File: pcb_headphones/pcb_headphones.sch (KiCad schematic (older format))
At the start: 32 parts, among them J1 CONN_01X03, J2 CONN_01X03, J3 CONN_01X03, J4 CONN_01X02, Q1 TIP121, U1 MC34063, U2 TDA2822M

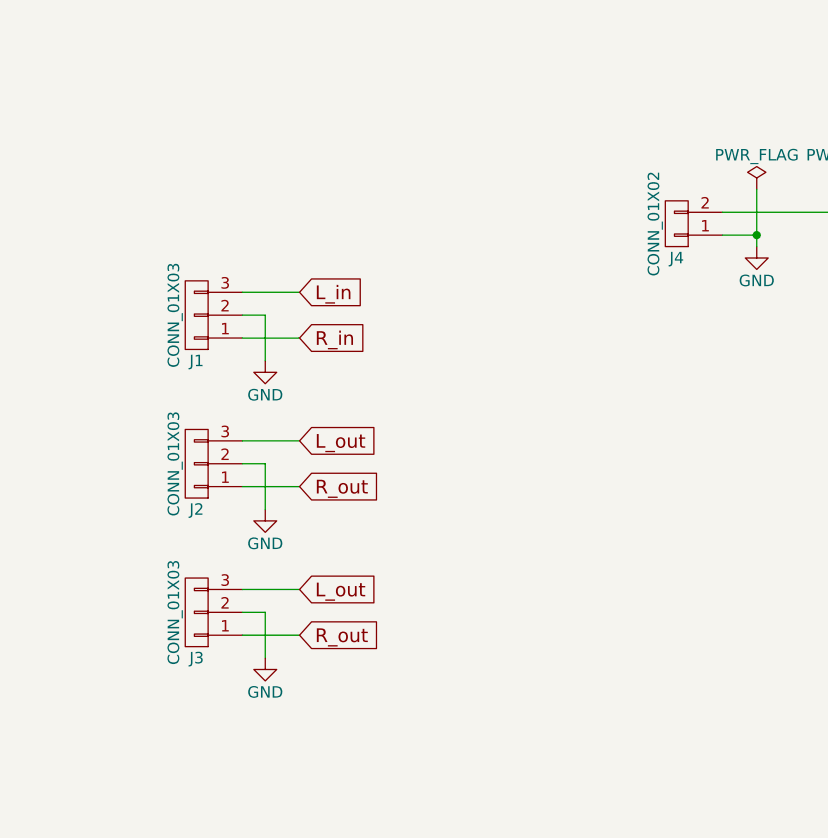
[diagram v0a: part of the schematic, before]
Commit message: Name connectors
Signed-off-by: Jan Losinski <losinski@wh2.tu-dresden.de>
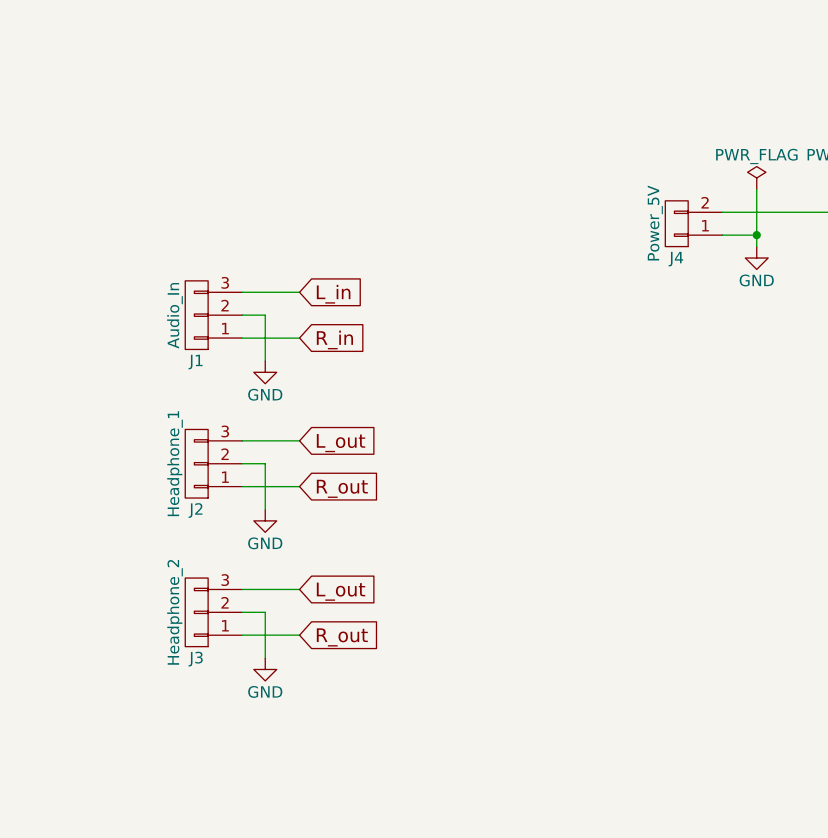
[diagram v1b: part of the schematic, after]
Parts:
- J1: value CONN_01X03 -> Audio_In
- J2: value CONN_01X03 -> Headphone_1
- J3: value CONN_01X03 -> Headphone_2
- J4: value CONN_01X02 -> Power_5V
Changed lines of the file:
@@
 P 6900 3650
 F 0 "J1" H 6900 3850 50  0000 C CNN
-F 1 "CONN_01X03" V 7000 3650 50  0000 C CNN
+F 1 "Audio_In" V 7000 3650 50  0000 C CNN
 F 2 "Pin_Headers:Pin_Header_Straight_1x03" H 6900 3650 50  0001 C CNN
 F 3 "" H 6900 3650 50  0001 C CNN
@@
 P 6900 4300
 F 0 "J2" H 6900 4500 50  0000 C CNN
-F 1 "CONN_01X03" V 7000 4300 50  0000 C CNN
+F 1 "Headphone_1" V 7000 4300 50  0000 C CNN
 F 2 "Pin_Headers:Pin_Header_Straight_1x03" H 6900 4300 50  0001 C CNN
 F 3 "" H 6900 4300 50  0001 C CNN
@@
 P 6900 4950
 F 0 "J3" H 6900 5150 50  0000 C CNN
-F 1 "CONN_01X03" V 7000 4950 50  0000 C CNN
+F 1 "Headphone_2" V 7000 4950 50  0000 C CNN
 F 2 "Pin_Headers:Pin_Header_Straight_1x03" H 6900 4950 50  0001 C CNN
 F 3 "" H 6900 4950 50  0001 C CNN
@@
 P 9000 3250
 F 0 "J4" H 9000 3400 50  0000 C CNN
-F 1 "CONN_01X02" V 9100 3250 50  0000 C CNN
+F 1 "Power_5V" V 9100 3250 50  0000 C CNN
 F 2 "Pin_Headers:Pin_Header_Straight_1x02" H 9000 3250 50  0001 C CNN
 F 3 "" H 9000 3250 50  0001 C CNN

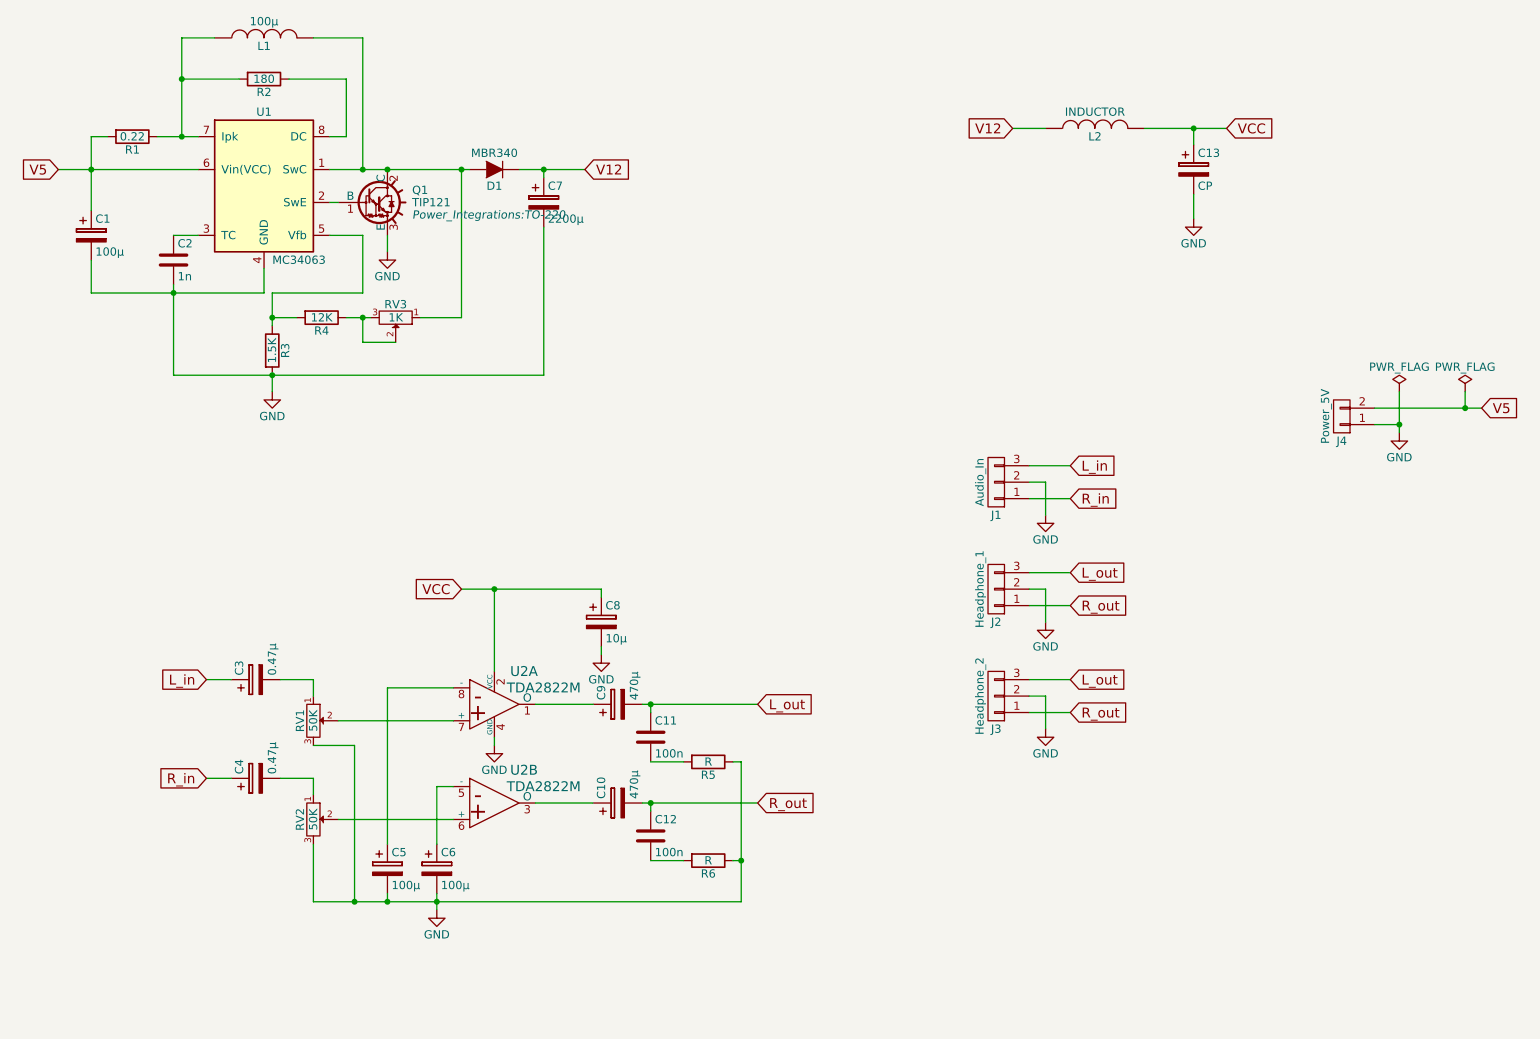
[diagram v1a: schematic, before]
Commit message: Rearange schematic
Signed-off-by: Jan Losinski <losinski@wh2.tu-dresden.de>
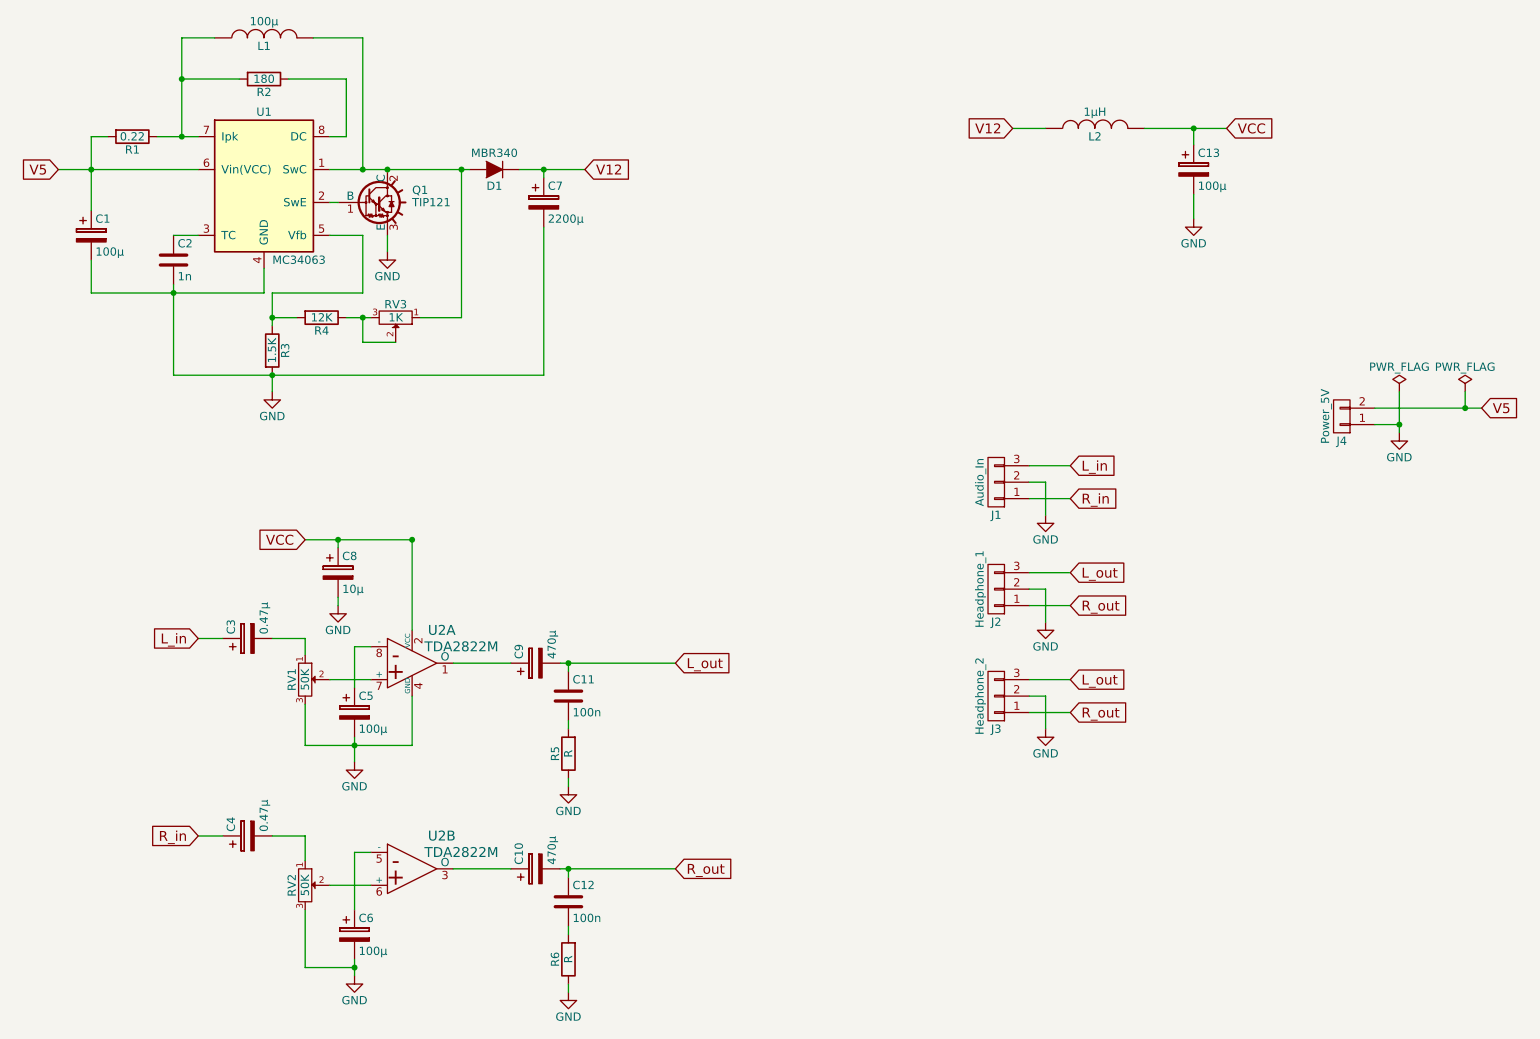
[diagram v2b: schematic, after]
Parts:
- C13: value CP -> 100µ
- L2: value INDUCTOR -> 1µH
- Q1: footprint Power_Integrations:TO-220 -> TO_SOT_Packages_THT:TO-220_Neutral123_Vertical
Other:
- moved on the sheet: C10, C11, C12, C3, C4, C5, C6, C8, C9, R5, R6, RV1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

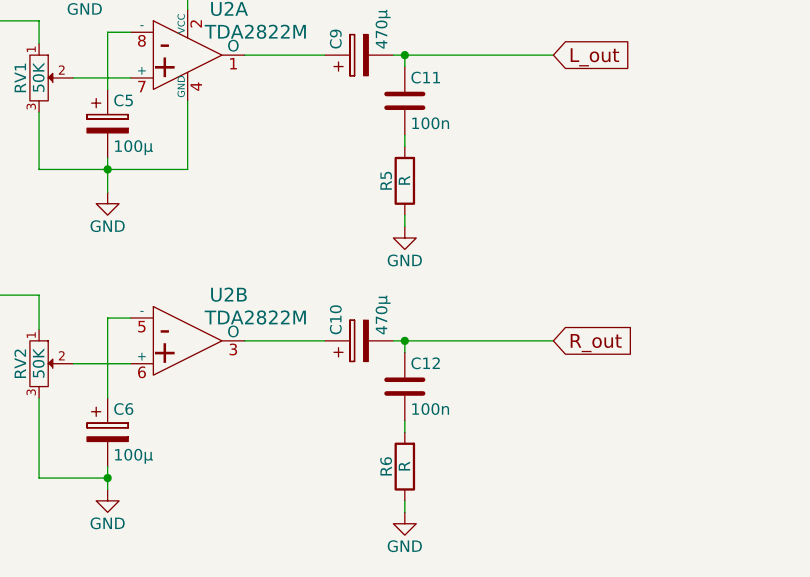
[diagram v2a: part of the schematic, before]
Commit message: Add missing resistor value
Signed-off-by: Jan Losinski <losinski@wh2.tu-dresden.de>
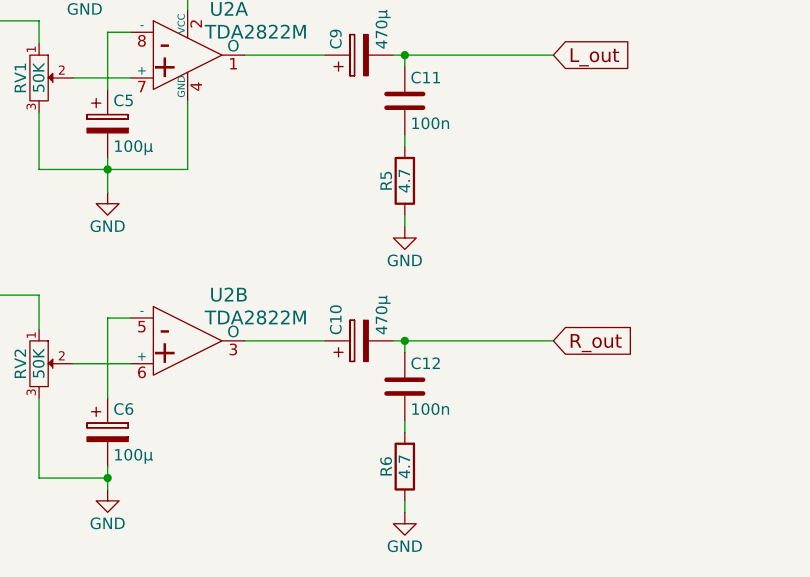
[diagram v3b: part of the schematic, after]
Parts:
- R5, R6: value R -> 4.7
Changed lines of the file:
@@
 P 4300 5300
 F 0 "R5" V 4380 5300 50  0000 C CNN
-F 1 "R" V 4300 5300 50  0000 C CNN
+F 1 "4.7" V 4300 5300 50  0000 C CNN
 F 2 "" V 4230 5300 50  0001 C CNN
 F 3 "" H 4300 5300 50  0000 C CNN
@@
 P 4300 6550
 F 0 "R6" V 4380 6550 50  0000 C CNN
-F 1 "R" V 4300 6550 50  0000 C CNN
+F 1 "4.7" V 4300 6550 50  0000 C CNN
 F 2 "" V 4230 6550 50  0001 C CNN
 F 3 "" H 4300 6550 50  0000 C CNN
